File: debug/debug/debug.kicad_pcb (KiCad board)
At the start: 2 copper layers, 175 x 125 mm, 2 parts

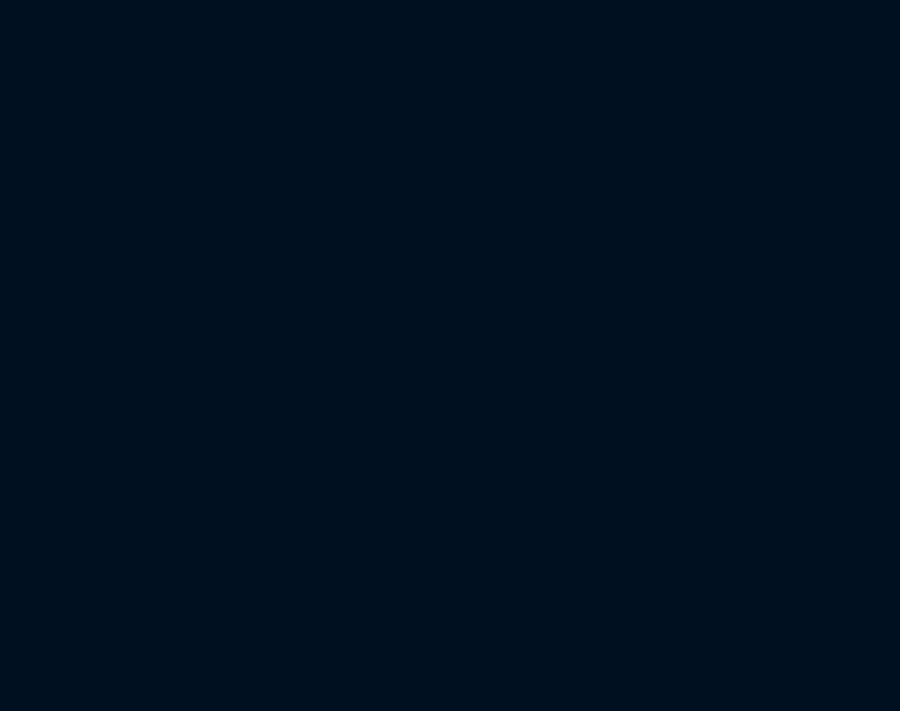
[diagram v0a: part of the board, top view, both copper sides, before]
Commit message: Added hierarchial blocks.
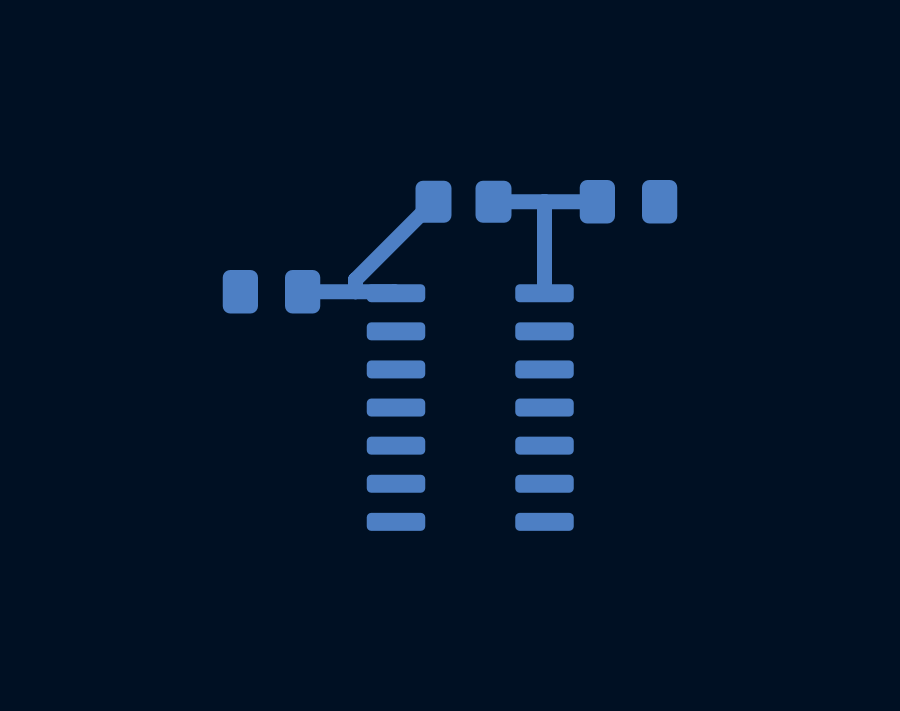
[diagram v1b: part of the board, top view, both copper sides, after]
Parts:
- added C1: 10uF, Capacitor_SMD:C_0805_2012Metric_Pad1.18x1.45mm_HandSolder, B.Cu at (94.0, 102.9)
- added C2: 100nF, Capacitor_SMD:C_0805_2012Metric_Pad1.18x1.45mm_HandSolder, B.Cu at (82.1, 105.9)
- added R1: 10k, Resistor_SMD:R_0805_2012Metric_Pad1.20x1.40mm_HandSolder, B.Cu at (88.5, 102.9)
- added U3: 74HCT74, Package_SO:SOIC-14_3.9x8.7mm_P1.27mm, B.Cu at (88.7, 109.8)
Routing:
- net 5v: track 0.00 -> 7.21 mm
- net Net-(U3A-~{R}): track 0.00 -> 6.51 mm
